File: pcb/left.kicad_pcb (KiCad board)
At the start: 2 copper layers, 190.5 x 125.7 mm, 78 parts, among them J1 OLED_CONN, K1 KEY_ESC, K10 KEY_Z, K11 KEY_LSUP, K12 KEY_W, K13 KEY_S, K14 KEY_X, K15 KEY_LALT, K16 KEY_3, K17 KEY_E, K18 KEY_D, K19 KEY_C, K2 KEY_1, K20 KEY_TL1, K21 KEY_4, K22 KEY_R, K23 KEY_F, K24 KEY_V, K25 KEY_TL2, K26 KEY_5, K27 KEY_T, K28 KEY_G, K29 KEY_B, K3 KEY_2, K30 KEY_TL3, K31 KEY_6, K32 KEY_CL1, K33 KEY_CL2, K34 KEY_CL3, K4 KEY_TAB, K5 KEY_CAPS, K6 KEY_LSFT, K7 KEY_LCTL, K8 KEY_Q, K9 KEY_A, U1 TRRS, U2 ProMicro

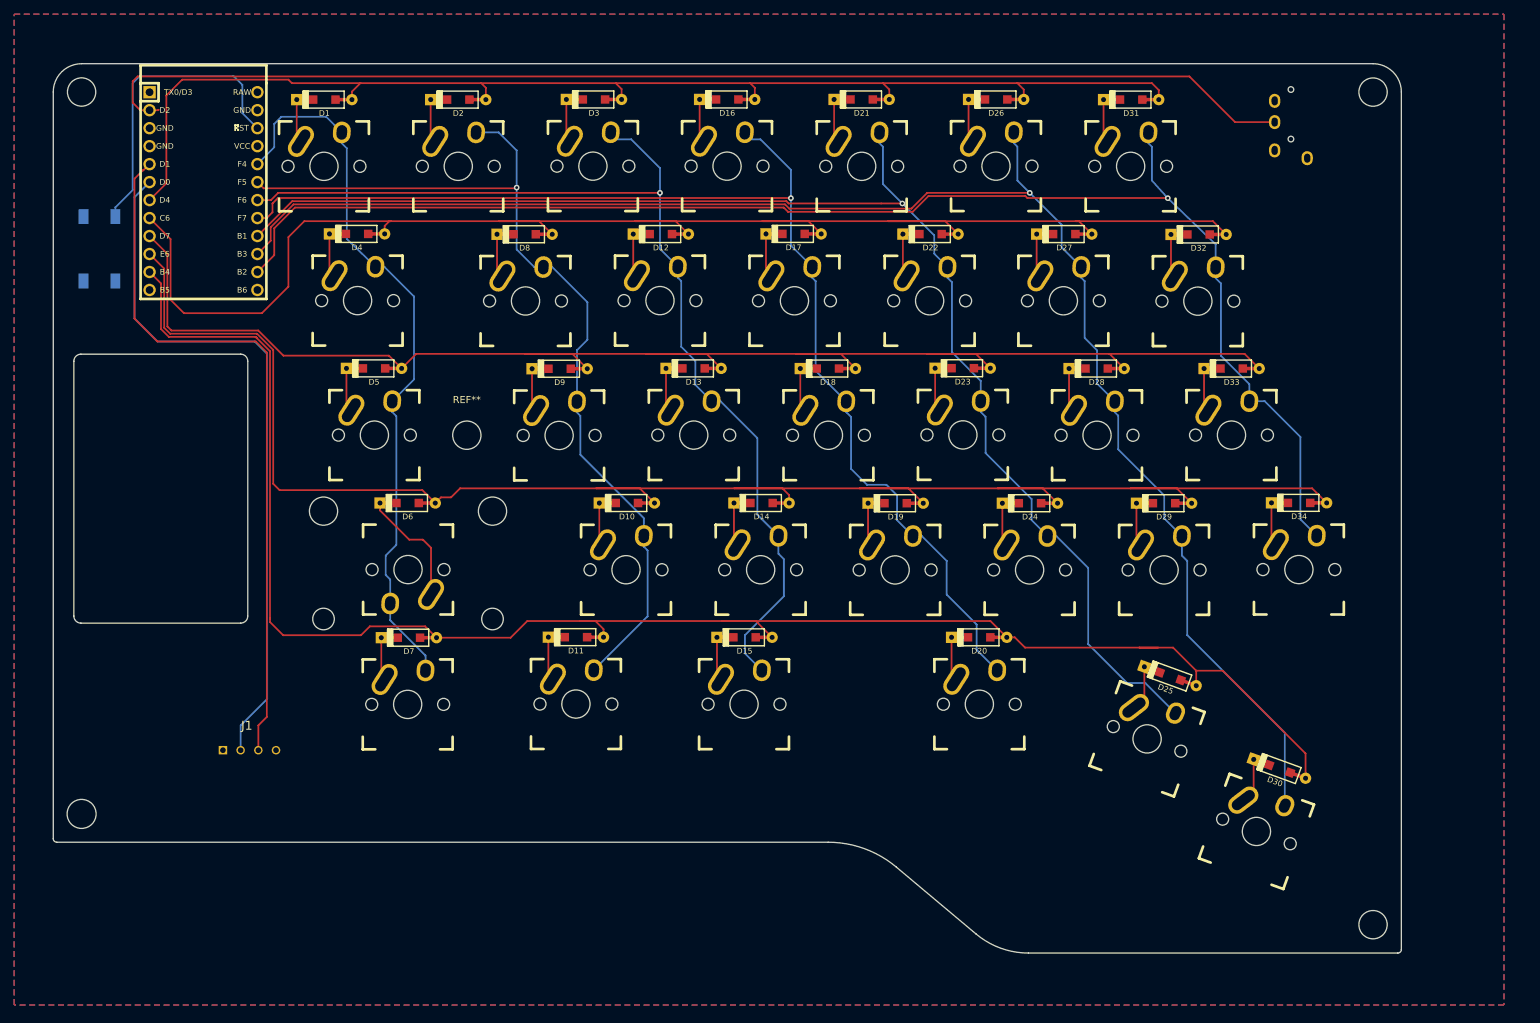
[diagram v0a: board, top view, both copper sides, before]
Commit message: Starting to wire left side
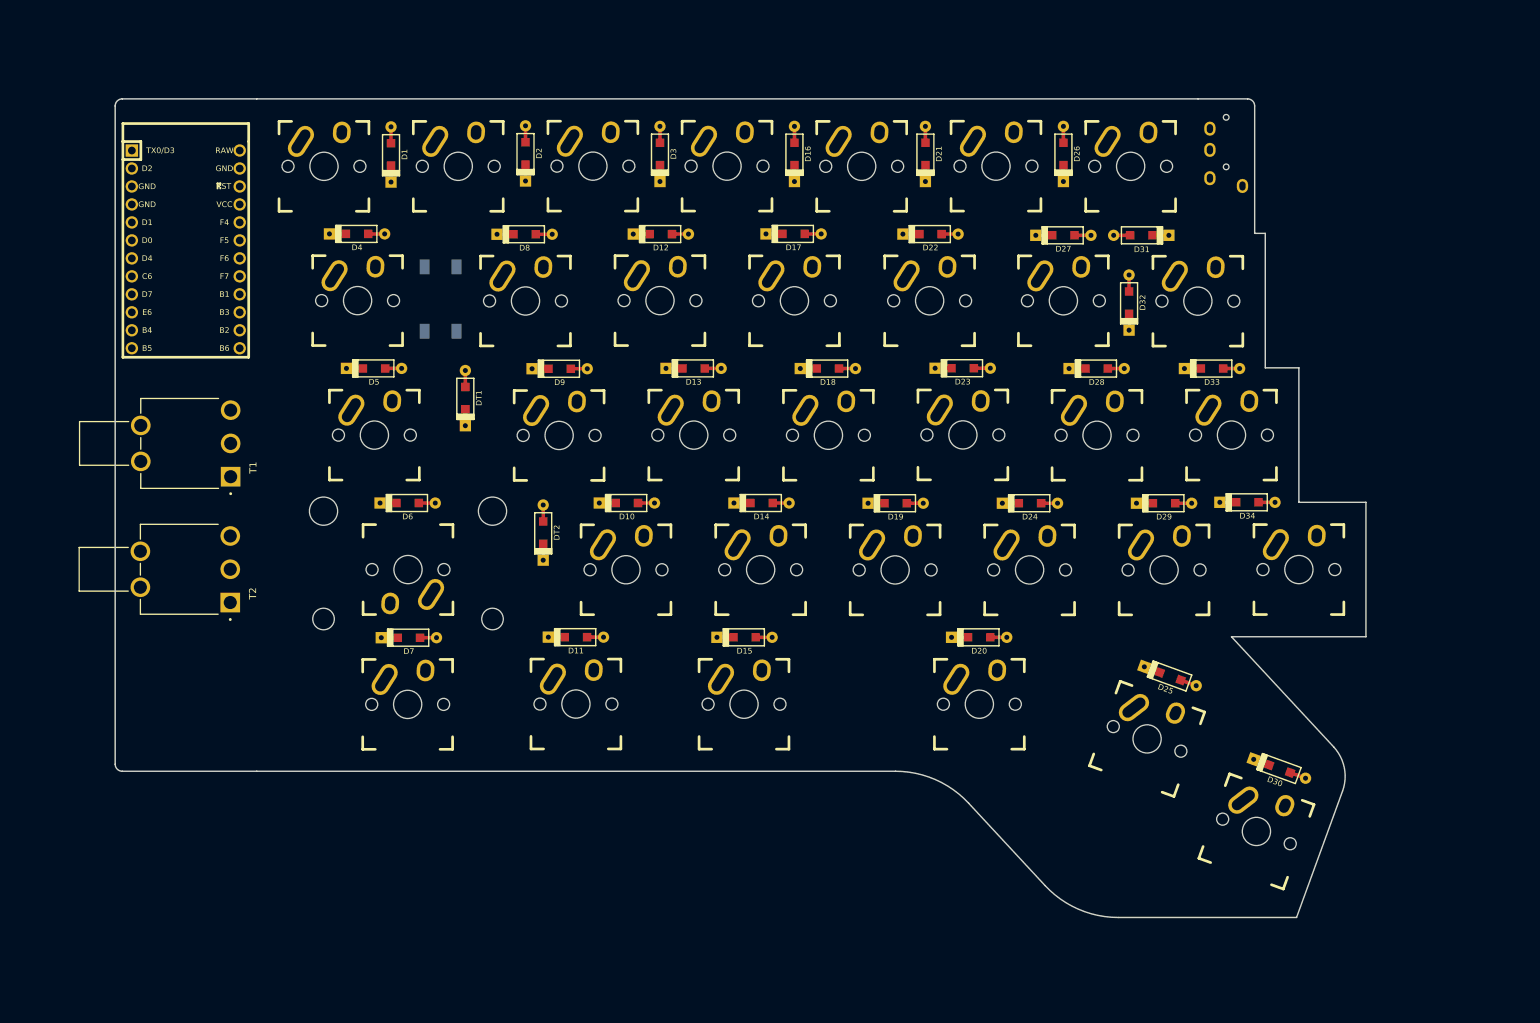
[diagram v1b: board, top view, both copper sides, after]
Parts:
- removed  : MountingHole_4mm, MountingHole:MountingHole_4mm (x4)
- removed J1: OLED_CONN, mouser:SHDR4W60P0X250_1X4_1240X1150X670P
- removed REF**: MountingHole_4mm, MountingHole:MountingHole_4mm
- added DT1: D_TMOD, keyboard_parts:D_SOD123_axial, F.Cu at (86.5, 72.0)
- added DT2: D_TSPC, keyboard_parts:D_SOD123_axial, F.Cu at (97.5, 91.0)
- added T1: T_MODE, toggle:SW_100SP1T2B4M6QE, F.Cu at (53.3, 78.4)
- added T2: T_SPACE, toggle:SW_100SP1T2B4M6QE, F.Cu at (53.3, 96.2)
- moved S1 48.7 mm to (83.0, 58.0)
- moved D31 19.2 mm to (182.0, 49.0), turned to 180 degrees
- moved D32 13.8 mm to (180.3, 58.5), turned to 90 degrees
- moved D16 12.2 mm to (133.0, 37.5), turned to 90 degrees
- moved D26 12.2 mm to (171.0, 37.5), turned to 90 degrees
- moved D1 12.2 mm to (76.0, 37.6), turned to 90 degrees
- moved D2 12.2 mm to (95.0, 37.4), turned to 90 degrees
- moved D3 12.1 mm to (114.0, 37.5), turned to 90 degrees
- moved D21 11.8 mm to (151.5, 37.5), turned to 90 degrees
- moved U1 9.96 mm to (194.0, 30.7)
- moved U2 8.61 mm to (47.0, 51.0)
- moved D34 7.30 mm to (197.0, 86.7)
- moved D33 2.78 mm to (192.0, 67.8)
- moved D27 0.22 mm to (171.0, 49.0)
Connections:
- net /GND renamed GND
- net /VCC renamed VCC
- K1 pad 2: /col0 -> /col1
- K10 pad 2: /col1 -> /col2
- K11 pad 2: /col1 -> /col2
- K12 pad 2: /col2 -> /col3
- K13 pad 2: /col2 -> /col3
- K14 pad 2: /col2 -> /col3
- K15 pad 2: /col2 -> /col3
- K16 pad 2: /col3 -> /col4
- K17 pad 2: /col3 -> /col4
- K18 pad 2: /col3 -> /col4
- K19 pad 2: /col3 -> /col4
- K2 pad 2: /col1 -> /col2
- K20 pad 2: /col3 -> /col4
- K21 pad 2: /col4 -> /col5
- K22 pad 2: /col4 -> /col5
- K23 pad 2: /col4 -> /col5
- K24 pad 2: /col4 -> /col5
- K25 pad 2: /col4 -> /col5
- K26 pad 2: /col5 -> /col6
- K27 pad 2: /col5 -> /col6
- K28 pad 2: /col5 -> /col6
- K29 pad 2: /col5 -> /col6
- K3 pad 2: /col2 -> /col3
- K30 pad 2: /col5 -> /col6
- K31 pad 2: /col6 -> /col7
- K32 pad 2: /col6 -> /col7
- K33 pad 2: /col6 -> /col7
- K34 pad 2: /col6 -> /col7
- K4 pad 2: /col0 -> /col1
- K5 pad 2: /col0 -> /col1
- K6 pad 2: /col0 -> /col1
- K7 pad 2: /col0 -> /col1
- K8 pad 2: /col1 -> /col2
- K9 pad 2: /col1 -> /col2
- S1 pad 1: Net-(S1-Pad1) -> unconnected-(S1-Pad1)
- S1 pad 3: Net-(S1-Pad3) -> unconnected-(S1-Pad3)
- U1 pad 4: Net-(U1-Pad4) -> unconnected-(U1-Pad4)
- U2 pad 1: Net-(U2-Pad1) -> unconnected-(U2-Pad1)
- U2 pad 12: Net-(U2-Pad12) -> unconnected-(U2-Pad12)
- U2 pad 13: Net-(U2-Pad13) -> /col7
- U2 pad 24: Net-(U2-Pad24) -> unconnected-(U2-Pad24)
- U2 pad 5: /SDA -> unconnected-(U2-Pad5)
- U2 pad 6: /SCL -> unconnected-(U2-Pad6)
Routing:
- net /row3: track 245.5 -> 0.00 mm
- net /row4: track 242.1 -> 0.00 mm
- net /col5: track 225.3 -> 0.00 mm, vias 1 -> 0
- net /row2: track 215.3 -> 0.00 mm
- net /row1: track 214.5 -> 0.00 mm
- net /col6: track 204.0 -> 0.00 mm, vias 1 -> 0
- net /col4: track 194.9 -> 0.00 mm, vias 1 -> 0
- net /row0: track 174.8 -> 0.00 mm
- net /serial: track 171.5 -> 0.00 mm
- net /col3: track 171.1 -> 0.00 mm, vias 1 -> 0
- net /col2: track 148.6 -> 0.00 mm, vias 1 -> 0
- net /col1: track 130.8 -> 0.00 mm, vias 1 -> 0
- net /col0: track 103.0 -> 0.00 mm
- net /SDA: track 100.1 -> 0.00 mm
- net /SCL: track 98.5 -> 0.00 mm
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- removed copper zone on B.Cu, net GND
- removed copper zone on F.Cu, net VCC
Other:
- board size 190.5 x 125.7 mm -> 176.7 x 115.7 mm
- net class Default removed

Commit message: Left pcb should be done
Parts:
- G***: moved to F.Cu
- U2: moved to B.Cu
- moved G*** 79.5 mm to (47.0, 113.0), turned to 0 degrees
- moved DT2 37.7 mm to (60.0, 95.0)
- moved DT1 26.9 mm to (60.0, 76.5)
- moved S1 0.30 mm to (83.0, 58.3), turned to -90 degrees
- turned D10 to 180 degrees
- turned D11 to 180 degrees
- turned D12 to 180 degrees
- turned D13 to 180 degrees
- turned D14 to 180 degrees
- turned D15 to 180 degrees
- turned D17 to 180 degrees
- turned D18 to 180 degrees
- turned D19 to 180 degrees
- turned D20 to 180 degrees
- turned D22 to 180 degrees
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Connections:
- U2 pad 13: /col7 -> /col0
- U2 pad 14: /col6 -> /col1
- U2 pad 15: /col5 -> /col2
- U2 pad 16: /col4 -> /col3
- U2 pad 17: /col3 -> /col4
- U2 pad 18: /col2 -> /col5
- U2 pad 19: /col1 -> /col6
- U2 pad 20: /col0 -> /col7
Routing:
- net /col6: track 0.00 -> 252.6 mm
- net /col7: track 0.00 -> 229.7 mm
- net /col5: track 0.00 -> 222.8 mm
- net /row4: track 0.00 -> 207.8 mm
- net /col4: track 0.00 -> 196.8 mm
- net /row3: track 0.00 -> 183.2 mm, vias 0 -> 1
- net /col3: track 0.00 -> 179.7 mm
- net VCC: track 0.00 -> 178.5 mm
- net /row0: track 0.00 -> 170.1 mm
- net /row2: track 0.00 -> 163.4 mm, vias 0 -> 1
- net /col2: track 0.00 -> 160.1 mm
- net /row1: track 0.00 -> 151.5 mm
- net /serial: track 0.00 -> 151.4 mm
- net /col1: track 0.00 -> 123.9 mm
- net /RST: track 0.00 -> 53.5 mm, vias 0 -> 2
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- added copper zone on B.Cu, net GND

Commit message: Starting on right pcb
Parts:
- U2: value ProMicro -> ProMicro USBC; footprint keebio:ArduinoProMicro -> keebio:ArduinoProMicro-USBC-Alibaba
- moved U2 1.01 mm to (47.0, 52.0)
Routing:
- net VCC: track 178.5 -> 176.4 mm
- net /serial: track 151.4 -> 152.9 mm
- net /RST: track 53.5 -> 52.3 mm
- net /col6: track 252.6 -> 253.7 mm
- net /col2: track 160.1 -> 161.1 mm
- net /row0: track 170.1 -> 171.1 mm
- net /col5: track 222.8 -> 223.8 mm
- net /col4: track 196.8 -> 197.8 mm
- net /row1: track 151.5 -> 152.5 mm
- net /col3: track 179.7 -> 180.7 mm

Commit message: Trying to add some fillets but something is messed up
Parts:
- U1: moved to F.Cu
- moved S1 22.7 mm to (60.5, 54.9)
- moved G*** 0.50 mm to (47.0, 113.5)
- turned U1 to 0 degrees
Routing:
- net /RST: track 52.3 -> 31.5 mm
- net GND: track 16.3 -> 2.34 mm, vias 0 -> 1
- net /serial: track 152.9 -> 160.1 mm, vias 0 -> 1
- net Net-(D31-Pad1): track 16.1 -> 18.3 mm
- net VCC: track 176.4 -> 177.2 mm
- net /row0: vias 0 -> 2
- added copper zone on F.Cu, net GND
- removed copper zone on B.Cu, net GND

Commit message: This is the version that I sent to manufacturers
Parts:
- moved T1 1.26 mm to (53.8, 77.2)
- moved U1 1.00 mm to (195.0, 30.7)
- moved T2 0.50 mm to (53.8, 96.2)
- moved G*** 0.50 mm to (47.5, 113.5)
- moved U2 0.50 mm to (47.5, 52.0)
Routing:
- net Net-(DT1-Pad1): track 7.78 -> 6.80 mm
- net /serial: track 160.1 -> 160.9 mm
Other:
- board size 176.7 x 115.7 mm -> 175.7 x 116.2 mm
- board text added: "JLCJLCJLCJLC"
